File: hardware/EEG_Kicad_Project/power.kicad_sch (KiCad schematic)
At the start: 10 parts, among them U2 TPS60403DBV

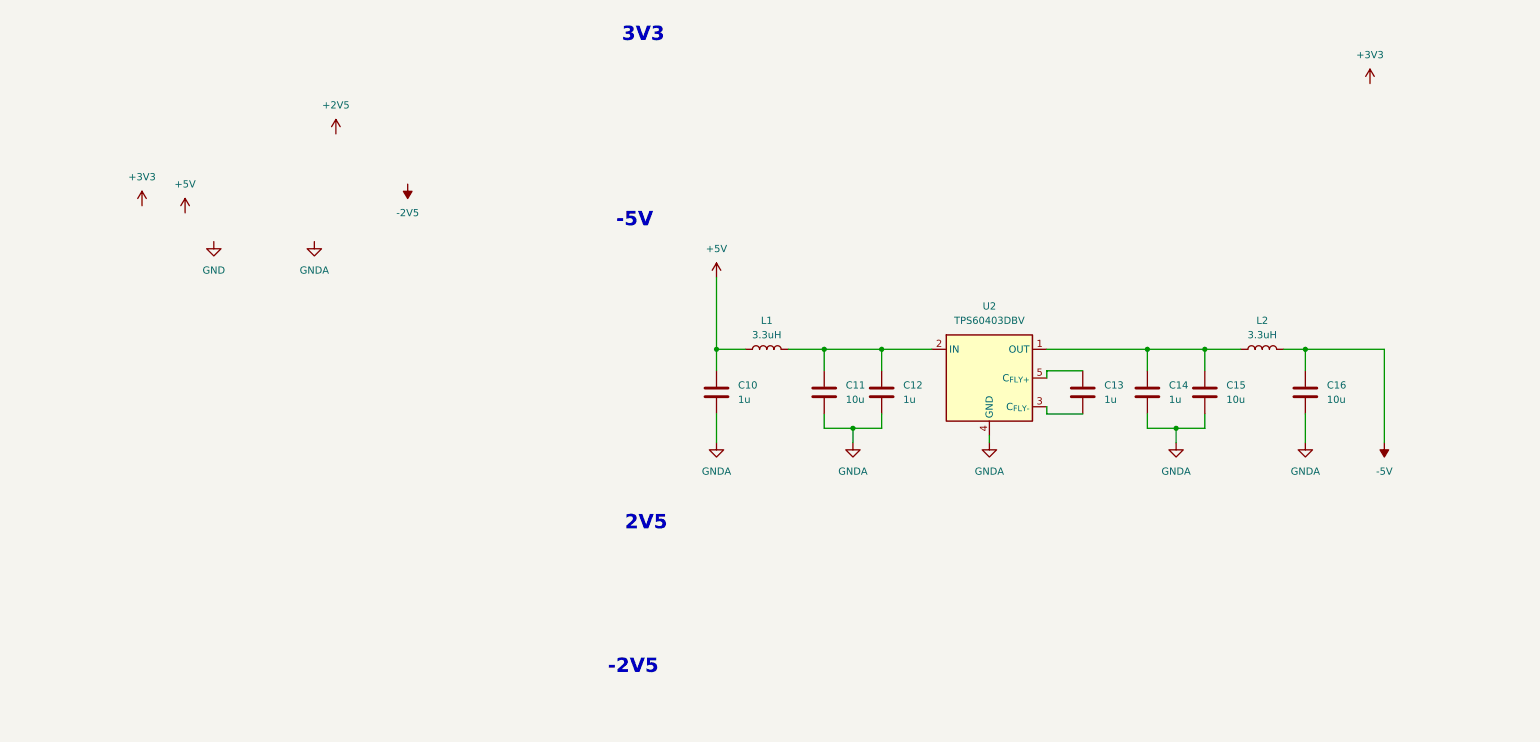
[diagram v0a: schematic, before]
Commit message: added power LDO IC's started routing
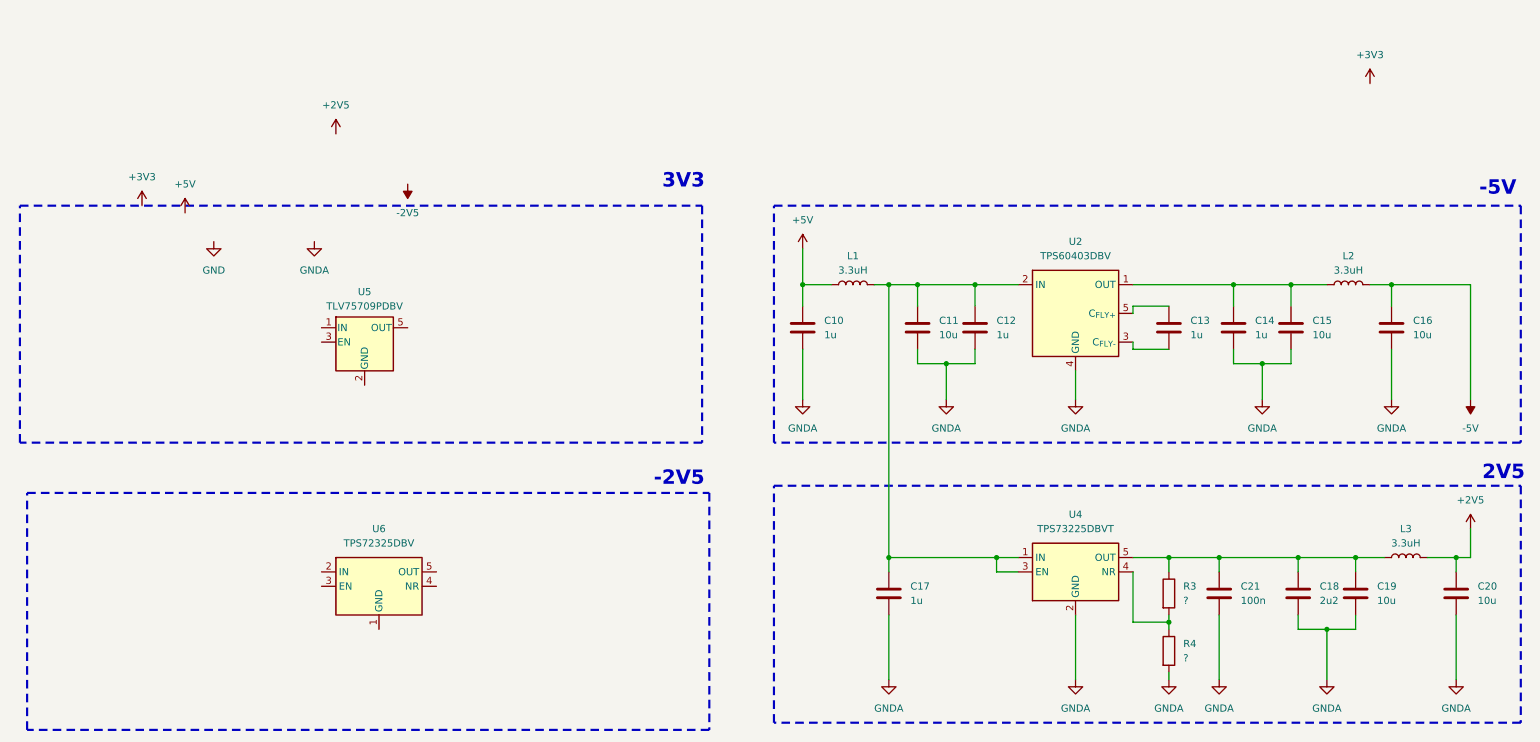
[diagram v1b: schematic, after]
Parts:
- added C17: 1u, Capacitor_SMD:C_0603_1608Metric, symbol Device:C
- added C18: 2u2, Capacitor_SMD:C_0603_1608Metric, symbol Device:C
- added C19, C20: 10u, Capacitor_SMD:C_0603_1608Metric, symbol Device:C
- added C21: 100n, Capacitor_SMD:C_0603_1608Metric, symbol Device:C
- added L3: 3.3uH, symbol Device:L
- added R3, R4: ?, symbol Device:R
- added U4: TPS73225DBVT, Package_TO_SOT_SMD:SOT-23-5, symbol Regulator_Linear:TPS73625DBV
- added U5: TLV75709PDBV, Package_TO_SOT_SMD:SOT-23-5, symbol Regulator_Linear:TLV75709PDBV
- added U6: TPS72325DBV, Package_TO_SOT_SMD:SOT-23-5, symbol Regulator_Linear:TPS72325DBV
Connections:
- net +2V5: now also C20.1, L3.2
- net GNDA: now also C17.2, C18.2, C19.2, C20.2, C21.2, R4.2, U4.2 (GND)
- net at C11.1, C12.1, L1.2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: now also C17.1, U4.1 (IN), U4.3 (EN)
- new net: R3.2, R4.1, U4.4 (NR)
- new net: C18.1, C19.1, C21.1, L3.1, R3.1, U4.5 (OUT)
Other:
- moved on the sheet: C10, C11, C12, C13, C14, C15, C16, L1, L2, U2

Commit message: added 3V3 /-2V5 wiring on schematic
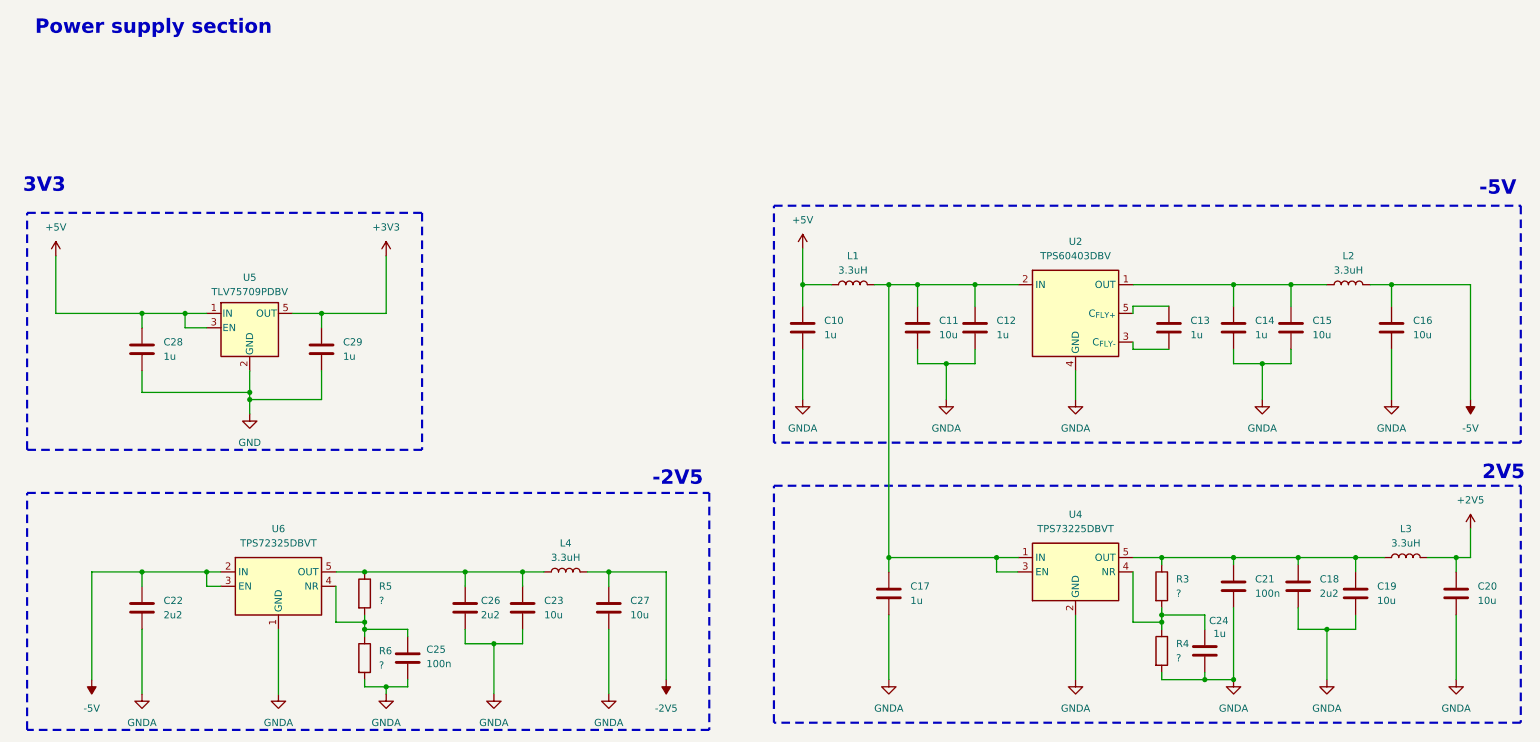
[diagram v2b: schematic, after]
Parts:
- added C22, C26: 2u2, Capacitor_SMD:C_0603_1608Metric, symbol Device:C
- added C23, C27: 10u, Capacitor_SMD:C_0603_1608Metric, symbol Device:C
- added C24, C28, C29: 1u, Capacitor_SMD:C_0603_1608Metric, symbol Device:C
- added C25: 100n, Capacitor_SMD:C_0603_1608Metric, symbol Device:C
- added L4: 3.3uH, symbol Device:L
- added R5, R6: ?, symbol Device:R
- U6: value TPS72325DBV -> TPS72325DBVT
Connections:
- net +3V3: now also U5.5 (OUT), C29.1
- net +5V: now also U5.1 (IN), U5.3 (EN), C28.1
- net -2V5: now also C27.1, L4.2
- net -5V: now also U6.2 (IN), U6.3 (EN), C22.1
- net GND: now also U5.2 (GND), C28.2, C29.2
- net GNDA: now also U6.1 (GND), C22.2, C23.2, C24.2, C25.2, C26.2, C27.2, R6.2
- net at R3.2, R4.1, U4.4 (NR): now also C24.1
- net at U6.4 (NR): now also C25.1, R5.2, R6.1
- net at U6.5 (OUT): now also C23.1, C26.1, L4.1, R5.1
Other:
- note added: "Power supply section"
- moved on the sheet: C18, C21, R3, R4, U5, U6
